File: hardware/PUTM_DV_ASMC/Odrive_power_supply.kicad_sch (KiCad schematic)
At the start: 24 parts, among them IC1 BTS722204ESAXUMA1

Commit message: done schematic v1
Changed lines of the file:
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@@
 	)
 	(hierarchical_label "OUTPUT_ODRIVE"
-		(shape input)
+		(shape output)
 		(at 189.23 71.12 0)
 		(effects

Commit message: schematic without error
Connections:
- net ODRIVE_1: now reaches C51.1, IC1.21 (OUT0_1), IC1.22 (OUT0_2), IC1.23 (OUT0_3), IC1.24 (OUT0_4)
- net ODRIVE_4: now reaches C54.1, IC1.13 (OUT3_1), IC1.14 (OUT3_2), IC1.15 (OUT3_3), IC1.16 (OUT3_4)
- net ODRIVE_3: now reaches C53.1, IC1.17 (OUT2_1), IC1.18 (OUT2_2)
- net ODRIVE_2: now reaches C52.1, IC1.19 (OUT1_1), IC1.20 (OUT1_2)
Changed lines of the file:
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@@
+		)
+	)
+	(label "ODRIVE_4"
+		(at 182.88 106.68 180)
+		(effects
+			(font
+				(size 1.27 1.27)
+			)
+			(justify right bottom)
+		)
+	)
+	(label "ODRIVE_1"
+		(at 182.88 78.74 180)
+		(effects
+			(font
+				(size 1.27 1.27)
+			)
+			(justify right bottom)
 		)
 	)
@@
 		)
 	)
+	(label "ODRIVE_2"
+		(at 182.88 88.9 180)
+		(effects
+			(font
+				(size 1.27 1.27)
+			)
+			(justify right bottom)
+		)
+	)
 	(label "IN3"
 		(at 118.11 104.14 180)
@@
 			(font
 				(size 0.5 0.5)
+			)
+			(justify right bottom)
+		)
+	)
+	(label "ODRIVE_3"
+		(at 182.88 96.52 180)
+		(effects
+			(font
+				(size 1.27 1.27)
 			)
 			(justify right bottom)
@@
 		)
 	)
-	(hierarchical_label "OUTPUT_ODRIVE"
+	(hierarchical_label "ODRIVE[1..4]"
 		(shape output)
 		(at 189.23 71.12 0)

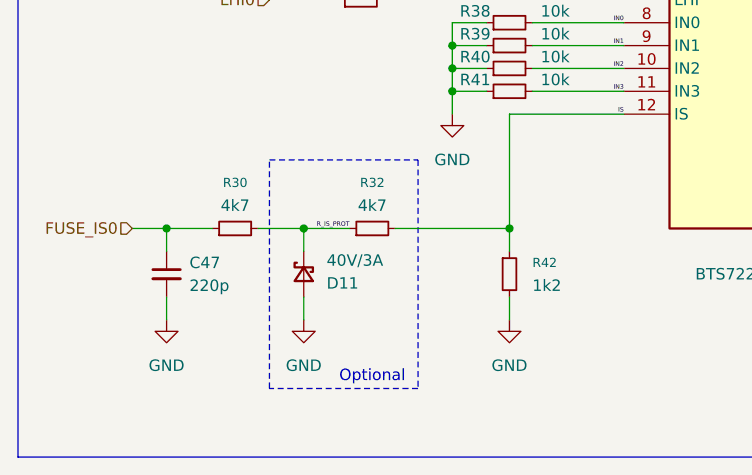
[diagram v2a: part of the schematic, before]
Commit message: tylko dwa bledy z can - schemat na wykonczeniu
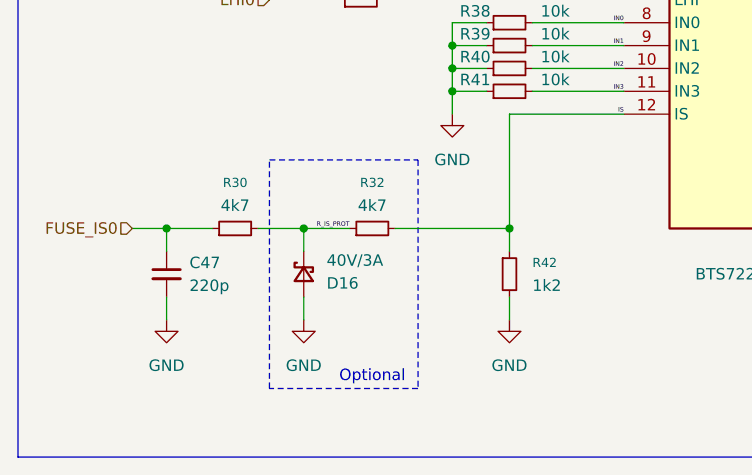
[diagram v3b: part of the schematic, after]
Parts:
- renumbered D11 to D16
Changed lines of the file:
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@@
 		(dnp no)
 		(fields_autoplaced yes)
-		(property "Reference" "#PWR066"
+		(property "Reference" "#PWR073"
 			(at 160.02 127 0)
 			(hide yes)
@@
 			(project "PUTM_DV_ASMC"
 				(path "/b652b05a-4e3d-4ad1-b032-18886abe7d45/df6a7f0c-3e94-451b-97ae-08b4f03339fc/45896247-8dc3-4df0-b7dc-f38cb46369bd"
-					(reference "#PWR066")
+					(reference "#PWR073")
 					(unit 1)
 				)
@@
 		(dnp no)
 		(fields_autoplaced yes)
-		(property "Reference" "#PWR062"
+		(property "Reference" "#PWR069"
 			(at 82.55 135.89 0)
 			(hide yes)
@@
 			(project "PUTM_DV_ASMC"
 				(path "/b652b05a-4e3d-4ad1-b032-18886abe7d45/df6a7f0c-3e94-451b-97ae-08b4f03339fc/45896247-8dc3-4df0-b7dc-f38cb46369bd"
-					(reference "#PWR062")
+					(reference "#PWR069")
 					(unit 1)
 				)
@@
 		(dnp no)
 		(fields_autoplaced yes)
-		(property "Reference" "#PWR061"
+		(property "Reference" "#PWR068"
 			(at 78.74 82.55 0)
 			(hide yes)
@@
 			(project "PUTM_DV_ASMC"
 				(path "/b652b05a-4e3d-4ad1-b032-18886abe7d45/df6a7f0c-3e94-451b-97ae-08b4f03339fc/45896247-8dc3-4df0-b7dc-f38cb46369bd"
-					(reference "#PWR061")
+					(reference "#PWR068")
 					(unit 1)
 				)
@@
 		(dnp no)
 		(fields_autoplaced yes)
-		(property "Reference" "#PWR063"
+		(property "Reference" "#PWR070"
 			(at 99.06 113.03 0)
 			(hide yes)
@@
 			(project "PUTM_DV_ASMC"
 				(path "/b652b05a-4e3d-4ad1-b032-18886abe7d45/df6a7f0c-3e94-451b-97ae-08b4f03339fc/45896247-8dc3-4df0-b7dc-f38cb46369bd"
-					(reference "#PWR063")
+					(reference "#PWR070")
 					(unit 1)
 				)
@@
 		(dnp no)
 		(fields_autoplaced yes)
-		(property "Reference" "#PWR060"
+		(property "Reference" "#PWR067"
 			(at 67.31 135.89 0)
 			(hide yes)
@@
 			(project "PUTM_DV_ASMC"
 				(path "/b652b05a-4e3d-4ad1-b032-18886abe7d45/df6a7f0c-3e94-451b-97ae-08b4f03339fc/45896247-8dc3-4df0-b7dc-f38cb46369bd"
-					(reference "#PWR060")
+					(reference "#PWR067")
 					(unit 1)
 				)
@@
 		(dnp no)
 		(fields_autoplaced yes)
-		(property "Reference" "#PWR064"
+		(property "Reference" "#PWR071"
 			(at 102.87 77.47 0)
 			(hide yes)
@@
 			(project "PUTM_DV_ASMC"
 				(path "/b652b05a-4e3d-4ad1-b032-18886abe7d45/df6a7f0c-3e94-451b-97ae-08b4f03339fc/45896247-8dc3-4df0-b7dc-f38cb46369bd"
-					(reference "#PWR064")
+					(reference "#PWR071")
 					(unit 1)
 				)
@@
 		(in_pos_files yes)
 		(dnp no)
-		(property "Reference" "D11"
+		(property "Reference" "D16"
 			(at 85.09 125.4761 90)
 			(show_name no)
@@
 			(project "PUTM_DV_ASMC"
 				(path "/b652b05a-4e3d-4ad1-b032-18886abe7d45/df6a7f0c-3e94-451b-97ae-08b4f03339fc/45896247-8dc3-4df0-b7dc-f38cb46369bd"
-					(reference "D11")
+					(reference "D16")
 					(unit 1)
 				)
@@
 		(dnp no)
 		(fields_autoplaced yes)
-		(property "Reference" "#PWR065"
+		(property "Reference" "#PWR072"
 			(at 105.41 135.89 0)
 			(hide yes)
@@
 			(project "PUTM_DV_ASMC"
 				(path "/b652b05a-4e3d-4ad1-b032-18886abe7d45/df6a7f0c-3e94-451b-97ae-08b4f03339fc/45896247-8dc3-4df0-b7dc-f38cb46369bd"
-					(reference "#PWR065")
+					(reference "#PWR072")
 					(unit 1)
 				)

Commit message: poprawki footprint
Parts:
- IC1: footprint PDM:SOP65P600X115-25N -> BTS722204ESAXUMA1:SOP65P600X115-25N
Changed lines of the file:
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@@
 			)
 		)
-		(property "Footprint" "PDM:SOP65P600X115-25N"
+		(property "Footprint" "BTS722204ESAXUMA1:SOP65P600X115-25N"
 			(at 149.86 173.66 0)
 			(hide yes)

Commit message: work on supply and zones
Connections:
- net ODRIVE_1 renamed ODRIVE1
- net ODRIVE_2 renamed ODRIVE2
- net ODRIVE_3 renamed ODRIVE3
- net ODRIVE_4 renamed ODRIVE4
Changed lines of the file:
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@@
 		)
 	)
-	(label "ODRIVE_4"
+	(label "ODRIVE4"
 		(at 182.88 106.68 180)
 		(effects
@@
 		)
 	)
-	(label "ODRIVE_1"
+	(label "ODRIVE1"
 		(at 182.88 78.74 180)
 		(effects
@@
 		)
 	)
-	(label "ODRIVE_2"
+	(label "ODRIVE2"
 		(at 182.88 88.9 180)
 		(effects
@@
 		)
 	)
-	(label "ODRIVE_3"
+	(label "ODRIVE3"
 		(at 182.88 96.52 180)
 		(effects
